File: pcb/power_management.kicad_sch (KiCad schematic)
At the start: 34 parts, among them J3 USB C, J4 BATT, Q2 AO3400A, Q3 AO3401A, SW5 POWER, U4 BQ25619, U5 AP2112K-3.3

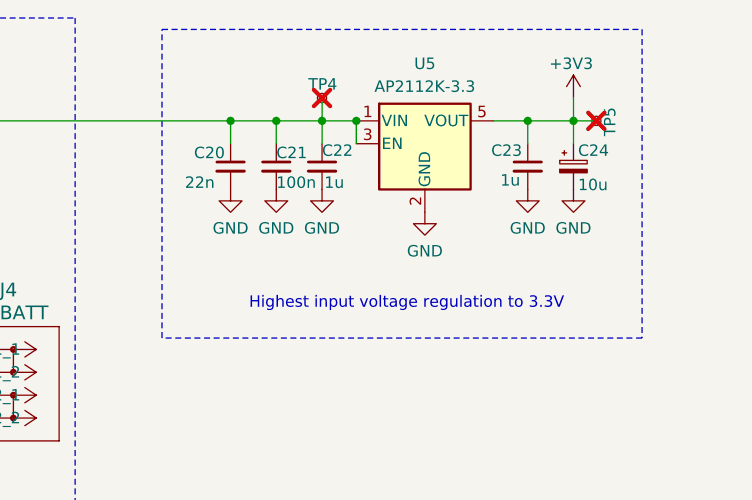
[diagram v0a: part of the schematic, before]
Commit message: a a solder jumper between power output and 3v3
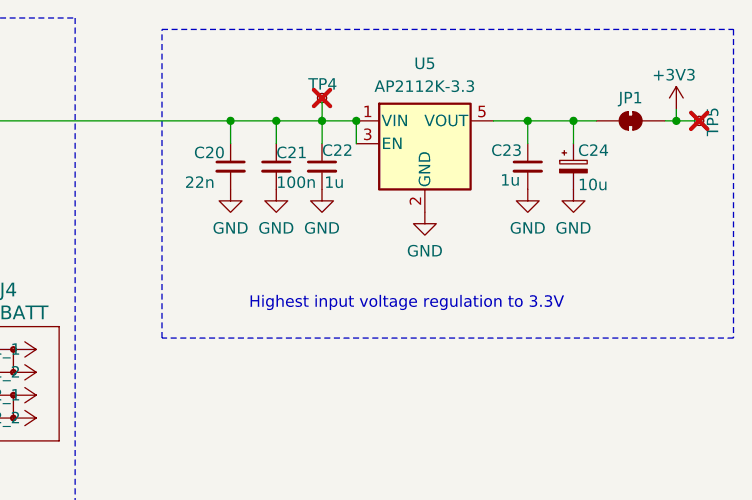
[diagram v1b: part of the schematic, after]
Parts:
- added JP1: SolderJumper_2_Bridged, Jumper:SolderJumper-2_P1.3mm_Bridged_RoundedPad1.0x1.5mm, symbol Jumper:SolderJumper_2_Bridged
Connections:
- net +3V3: now also JP1.2 (B); no longer C23.1, C24.1, U5.5 (VOUT)
- new net: C23.1, C24.1, JP1.1 (A), U5.5 (VOUT)
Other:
- moved on the sheet: TP5
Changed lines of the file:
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@@
 	(rectangle
 		(start 208.28 26.67)
-		(end 261.62 60.96)
+		(end 271.78 60.96)
 		(stroke
 			(width 0)
@@
 	)
 	(junction
+		(at 265.43 36.83)
+		(diameter 0)
+		(color 0 0 0 0)
+	)
+	(junction
 		(at 50.8 76.2)
 		(diameter 0)
@@
 	(wire
 		(pts
-			(xy 254 36.83) (xy 254 34.29)
+			(xy 166.37 53.34) (xy 166.37 54.61)
 		)
 		(stroke
@@
 	(wire
 		(pts
-			(xy 166.37 53.34) (xy 166.37 54.61)
+			(xy 265.43 36.83) (xy 267.97 36.83)
 		)
 		(stroke
@@
 	(wire
 		(pts
+			(xy 264.16 36.83) (xy 265.43 36.83)
+		)
+		(stroke
+			(width 0)
+			(type default)
+		)
+	)
+	(wire
+		(pts
 			(xy 254 36.83) (xy 254 39.37)
 		)
@@
 	(wire
 		(pts
+			(xy 265.43 35.56) (xy 265.43 36.83)
+		)
+		(stroke
+			(width 0)
+			(type default)
+		)
+	)
+	(wire
+		(pts
 			(xy 83.82 125.73) (xy 83.82 137.16)
 		)
@@
 	(symbol
 		(lib_id "power:+3V3")
-		(at 254 34.29 0)
+		(at 265.43 35.56 0)
 		(unit 1)
 		(exclude_from_sim no)
@@
 		(dnp no)
 		(property "Reference" "#PWR043"
-			(at 254 38.1 0)
+			(at 265.43 39.37 0)
 			(effects
 				(font
@@
 		)
 		(property "Value" "+3V3"
-			(at 253.746 30.48 0)
+			(at 265.176 31.75 0)
 			(effects
 				(font
@@
 		)
 		(property "Footprint" ""
-			(at 254 34.29 0)
+			(at 265.43 35.56 0)
 			(effects
 				(font
@@
 		)
 		(property "Datasheet" ""
-			(at 254 34.29 0)
+			(at 265.43 35.56 0)
 			(effects
 				(font
@@
 		)
 		(property "Description" "Power symbol creates a global label with name \"+3V3\""
-			(at 254 34.29 0)
+			(at 265.43 35.56 0)
 			(effects
 				(font
@@
 	)
 	(symbol
+		(lib_id "Jumper:SolderJumper_2_Bridged")
+		(at 260.35 36.83 0)
+		(unit 1)
+		(exclude_from_sim no)
+		(in_bom no)
+		(on_board yes)
+		(dnp no)
+		(property "Reference" "JP1"
+			(at 260.35 34.29 0)
+			(effects
+				(font
+					(size 1.27 1.27)
+				)
+			)
+		)
+		(property "Value" "SolderJumper_2_Bridged"
+			(at 260.35 33.02 0)
+			(effects
+				(font
+					(size 1.27 1.27)
+				)
+				(hide yes)
+			)
+		)
+		(property "Footprint" "Jumper:SolderJumper-2_P1.3mm_Bridged_RoundedPad1.0x1.5mm"
+			(at 260.35 36.83 0)
+			(effects
+				(font
+					(size 1.27 1.27)
+				)
+				(hide yes)
+			)
+		)
+		(property "Datasheet" "~"
+			(at 260.35 36.83 0)
+			(effects
+				(font
+					(size 1.27 1.27)
+				)
+				(hide yes)
+			)
+		)
+		(property "Description" "Solder Jumper, 2-pole, closed/bridged"
+			(at 260.35 36.83 0)
+			(effects
+				(font
+					(size 1.27 1.27)
+				)
+				(hide yes)
+			)
+		)
+		(pin "2"
+		)
+		(pin "1"
+		)
+		(instances
+			(project ""
+				(path "/e47b2519-93ca-4a48-9414-ecc253dd35f5/702fc064-eab2-4b82-8f62-a654ccd28f72"
+					(reference "JP1")
+					(unit 1)
+				)
+			)
+		)
+	)
+	(symbol
 		(lib_id "power:+3V3")
 		(at 128.27 49.53 0)
@@
 	(symbol
 		(lib_id "Connector:TestPoint_Small")
-		(at 256.54 36.83 270)
+		(at 267.97 36.83 270)
 		(unit 1)
 		(exclude_from_sim no)
@@
 		(dnp yes)
 		(property "Reference" "TP5"
-			(at 258.064 35.306 0)
+			(at 269.494 35.306 0)
 			(effects
 				(font
@@
 		)
 		(property "Value" "3.3V"
-			(at 255.2701 38.1 0)
+			(at 266.7001 38.1 0)
 			(effects
 				(font
@@
 		)
 		(property "Footprint" "leany_footprints:TestPoint_Pad_1.0x1.0mm"
-			(at 256.54 41.91 0)
+			(at 267.97 41.91 0)
 			(effects
 				(font
@@
 		)
 		(property "Datasheet" "~"
-			(at 256.54 41.91 0)
+			(at 267.97 41.91 0)
 			(effects
 				(font
@@
 		)
 		(property "Description" "test point"
-			(at 256.54 36.83 0)
+			(at 267.97 36.83 0)
 			(effects
 				(font
@@
 		)
 		(property "Category" ""
-			(at 256.54 36.83 0)
+			(at 267.97 36.83 0)
 			(effects
 				(font
@@
 		)
 		(property "DK_Datasheet_Link" ""
-			(at 256.54 36.83 0)
+			(at 267.97 36.83 0)
 			(effects
 				(font
@@
 		)
 		(property "DK_Detail_Page" ""
-			(at 256.54 36.83 0)
+			(at 267.97 36.83 0)
 			(effects
 				(font
@@
 		)
 		(property "Description_1" ""
-			(at 256.54 36.83 0)
+			(at 267.97 36.83 0)
 			(effects
 				(font
@@
 		)
 		(property "Digi-Key_PN" ""
-			(at 256.54 36.83 0)
+			(at 267.97 36.83 0)
 			(effects
 				(font
@@
 		)
 		(property "Family" ""
-			(at 256.54 36.83 0)
+			(at 267.97 36.83 0)
 			(effects
 				(font
@@
 		)
 		(property "LCSC" ""
-			(at 256.54 36.83 0)
+			(at 267.97 36.83 0)
 			(effects
 				(font
@@
 		)
 		(property "MPN" ""
-			(at 256.54 36.83 0)
+			(at 267.97 36.83 0)
 			(effects
 				(font
@@
 		)
 		(property "Manufacturer" ""
-			(at 256.54 36.83 0)
+			(at 267.97 36.83 0)
 			(effects
 				(font
@@
 		)
 		(property "Status" ""
-			(at 256.54 36.83 0)
+			(at 267.97 36.83 0)
 			(effects
 				(font

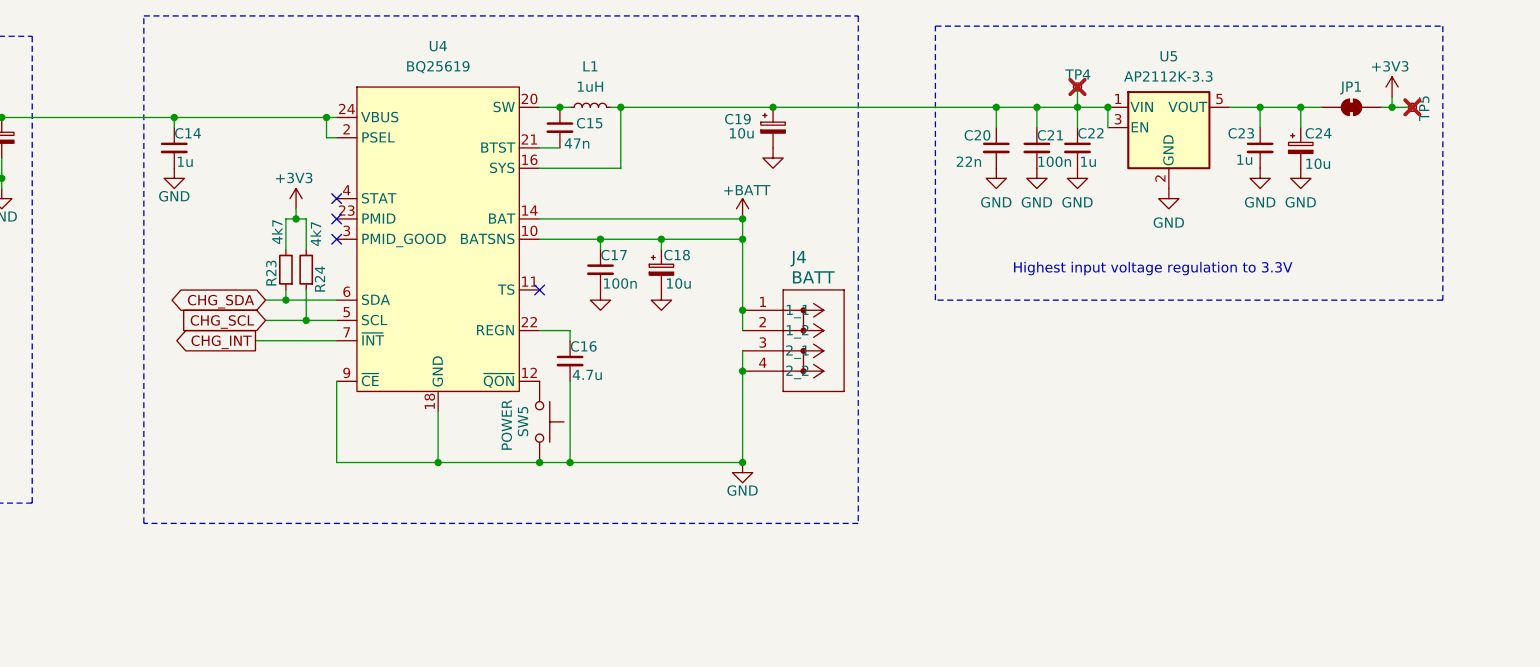
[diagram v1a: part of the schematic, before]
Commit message: add a reverse-voltage protection mosfet
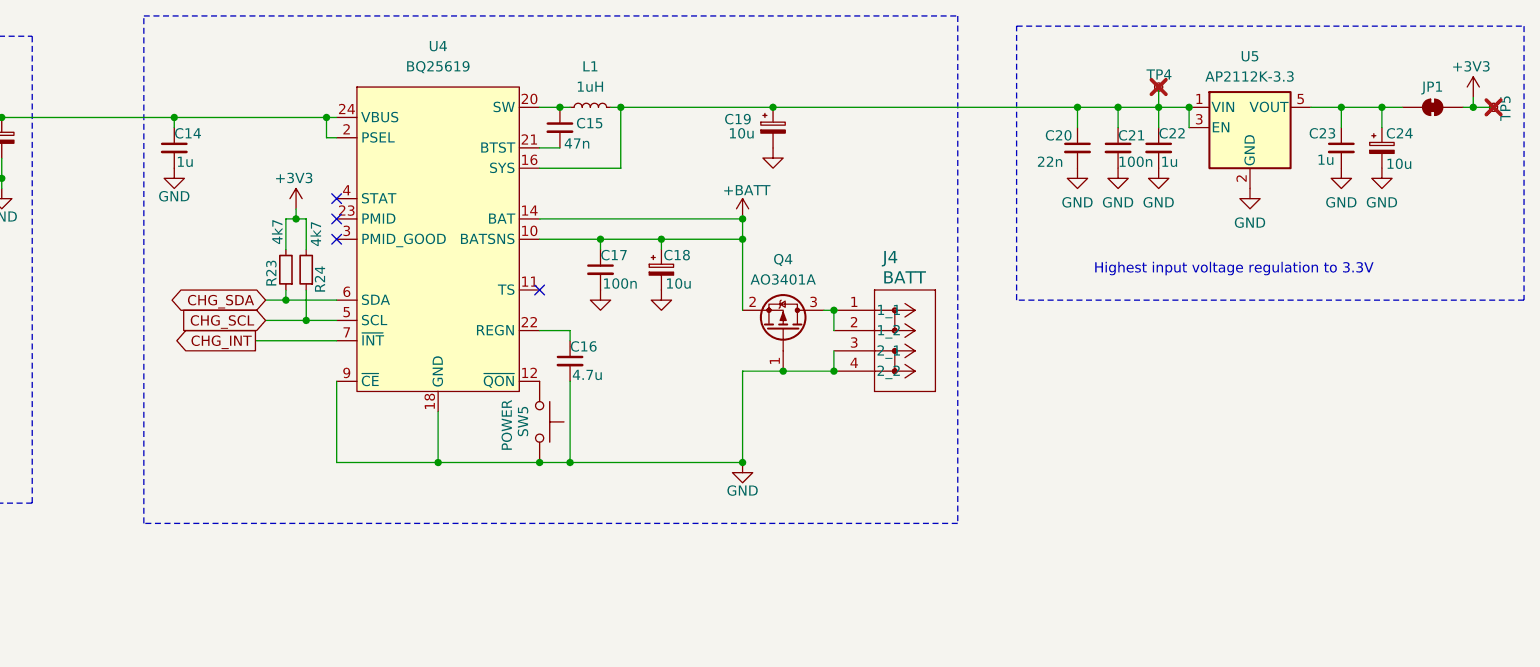
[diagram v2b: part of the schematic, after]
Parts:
- added Q4: AO3401A, Package_TO_SOT_SMD:SOT-23, symbol Transistor_FET:AO3401A
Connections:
- net +BATT: now also Q4.2 (S); no longer J4.1 (1_1), J4.2 (1_2)
- net GND: now also Q4.1 (G)
- new net: J4.1 (1_1), J4.2 (1_2), Q4.3 (D)
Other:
- moved on the sheet: C20, C21, C22, C23, C24, J4, JP1, TP4, TP5, U5

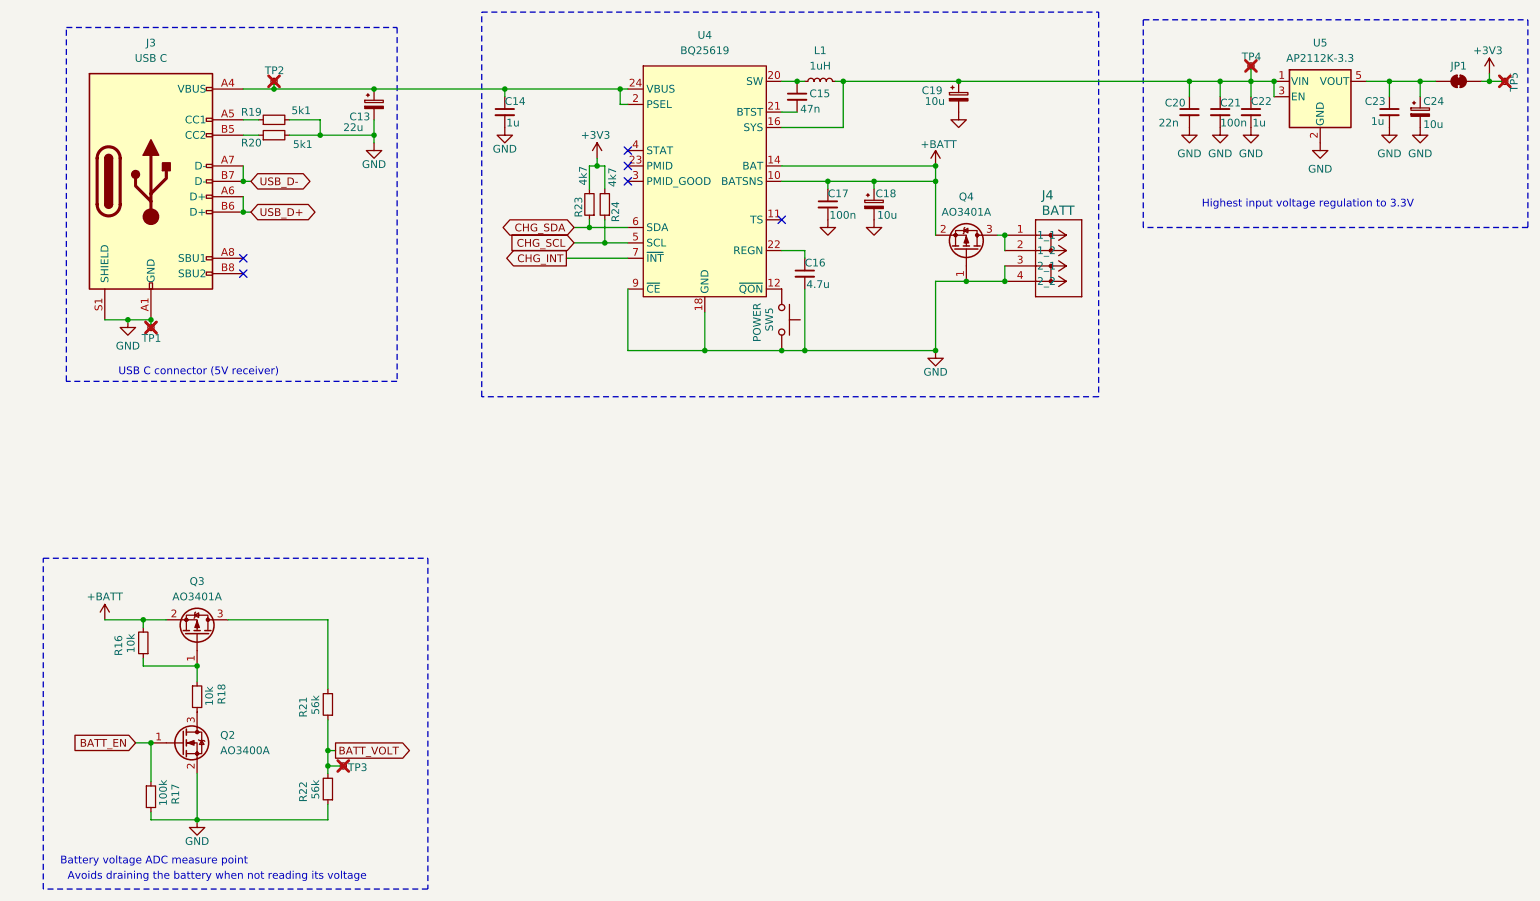
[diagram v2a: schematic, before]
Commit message: replace solder jumper by a test pad near battery
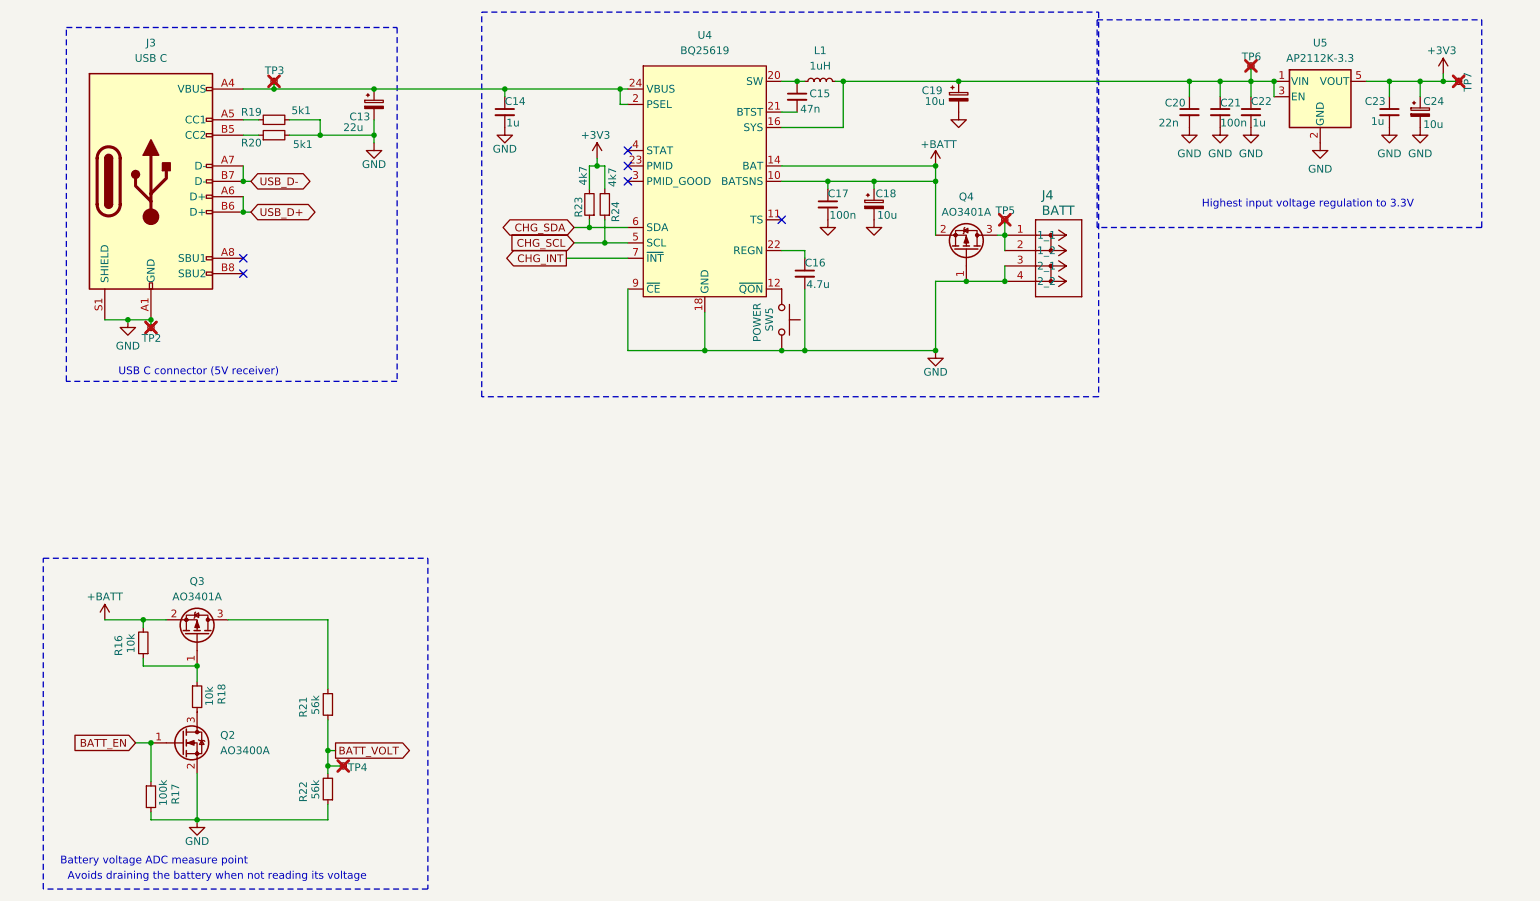
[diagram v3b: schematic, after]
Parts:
- removed JP1: SolderJumper_2_Bridged, Jumper:SolderJumper-2_P1.3mm_Bridged_RoundedPad1.0x1.5mm, symbol Jumper:SolderJumper_2_Bridged
- added TP5: 3.3V, leany_footprints:TestPoint_Pad_1.0x1.0mm, symbol Connector:TestPoint_Small
- renumbered TP1 to TP2, TP2 to TP3, TP3 to TP4, TP4 to TP6, TP5 to TP7
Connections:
- net +3V3: now also C23.1, C24.1, U5.5 (VOUT)
- net at J4.1 (1_1), J4.2 (1_2), Q4.3 (D): now also TP5.1
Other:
- moved on the sheet: TP7

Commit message: start re-designing PCB to 4 layers
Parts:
- C14, C15, C17, C20, C21, C22, C23: footprint Capacitor_SMD:C_0603_1608Metric -> Capacitor_SMD:C_0402_1005Metric
- R16, R17, R18, R19, R20, R21, R22, R23, R24: footprint Resistor_SMD:R_0603_1608Metric -> Resistor_SMD:R_0402_1005Metric
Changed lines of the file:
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@@
 			)
 		)
-		(property "Footprint" "Resistor_SMD:R_0603_1608Metric"
+		(property "Footprint" "Resistor_SMD:R_0402_1005Metric"
 			(at 74.93 43.18 0)
 			(effects
@@
 			)
 		)
-		(property "Footprint" "Capacitor_SMD:C_0603_1608Metric"
+		(property "Footprint" "Capacitor_SMD:C_0402_1005Metric"
 			(at 231.14 41.91 0)
 			(effects
@@
 			)
 		)
-		(property "Footprint" "Resistor_SMD:R_0603_1608Metric"
+		(property "Footprint" "Resistor_SMD:R_0402_1005Metric"
 			(at 83.82 153.67 0)
 			(effects
@@
 			)
 		)
-		(property "Footprint" "Resistor_SMD:R_0603_1608Metric"
+		(property "Footprint" "Resistor_SMD:R_0402_1005Metric"
 			(at 54.61 154.94 0)
 			(effects
@@
 			)
 		)
-		(property "Footprint" "Resistor_SMD:R_0603_1608Metric"
+		(property "Footprint" "Resistor_SMD:R_0402_1005Metric"
 			(at 62.23 138.43 0)
 			(effects
@@
 			)
 		)
-		(property "Footprint" "Capacitor_SMD:C_0603_1608Metric"
+		(property "Footprint" "Capacitor_SMD:C_0402_1005Metric"
 			(at 113.03 41.91 0)
 			(effects
@@
 			)
 		)
-		(property "Footprint" "Resistor_SMD:R_0603_1608Metric"
+		(property "Footprint" "Resistor_SMD:R_0402_1005Metric"
 			(at 83.82 139.7 0)
 			(effects
@@
 			)
 		)
-		(property "Footprint" "Resistor_SMD:R_0603_1608Metric"
+		(property "Footprint" "Resistor_SMD:R_0402_1005Metric"
 			(at 74.93 45.72 0)
 			(effects
@@
 			)
 		)
-		(property "Footprint" "Resistor_SMD:R_0603_1608Metric"
+		(property "Footprint" "Resistor_SMD:R_0402_1005Metric"
 			(at 127 57.15 0)
 			(effects
@@
 			)
 		)
-		(property "Footprint" "Capacitor_SMD:C_0603_1608Metric"
+		(property "Footprint" "Capacitor_SMD:C_0402_1005Metric"
 			(at 166.37 57.15 0)
 			(effects
@@
 			)
 		)
-		(property "Footprint" "Capacitor_SMD:C_0603_1608Metric"
+		(property "Footprint" "Capacitor_SMD:C_0402_1005Metric"
 			(at 236.22 41.91 0)
 			(effects
@@
 			)
 		)
-		(property "Footprint" "Capacitor_SMD:C_0603_1608Metric"
+		(property "Footprint" "Capacitor_SMD:C_0402_1005Metric"
 			(at 226.06 41.91 0)
 			(effects
@@
 			)
 		)
-		(property "Footprint" "Resistor_SMD:R_0603_1608Metric"
+		(property "Footprint" "Resistor_SMD:R_0402_1005Metric"
 			(at 53.34 129.54 0)
 			(effects
@@
 			)
 		)
-		(property "Footprint" "Resistor_SMD:R_0603_1608Metric"
+		(property "Footprint" "Resistor_SMD:R_0402_1005Metric"
 			(at 129.54 57.15 0)
 			(effects
@@
 			)
 		)
-		(property "Footprint" "Capacitor_SMD:C_0603_1608Metric"
+		(property "Footprint" "Capacitor_SMD:C_0402_1005Metric"
 			(at 161.29 39.37 0)
 			(effects
@@
 			)
 		)
-		(property "Footprint" "Capacitor_SMD:C_0603_1608Metric"
+		(property "Footprint" "Capacitor_SMD:C_0402_1005Metric"
 			(at 259.08 41.91 0)
 			(effects

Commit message: update resistors BOM
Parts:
- R16, R18: LCSC C25804 -> C25744
- R17: LCSC C25803 -> C25741
- R19, R20: LCSC C23186 -> C25905
- R21, R22: footprint Resistor_SMD:R_0402_1005Metric -> Resistor_SMD:R_0603_1608Metric
- R23, R24: LCSC C23162 -> C25900
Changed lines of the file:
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@@
 			)
 		)
-		(property "LCSC" "C23186"
+		(property "LCSC" "C25905"
 			(at 74.93 43.18 0)
 			(effects
@@
 			)
 		)
-		(property "Footprint" "Resistor_SMD:R_0402_1005Metric"
+		(property "Footprint" "Resistor_SMD:R_0603_1608Metric"
 			(at 83.82 153.67 0)
 			(effects
@@
 			)
 		)
-		(property "LCSC" "C25803"
+		(property "LCSC" "C25741"
 			(at 54.61 154.94 0)
 			(effects
@@
 			)
 		)
-		(property "LCSC" "C25804"
+		(property "LCSC" "C25744"
 			(at 62.23 138.43 0)
 			(effects
@@
 			)
 		)
-		(property "Footprint" "Resistor_SMD:R_0402_1005Metric"
+		(property "Footprint" "Resistor_SMD:R_0603_1608Metric"
 			(at 83.82 139.7 0)
 			(effects
@@
 			)
 		)
-		(property "LCSC" "C23186"
+		(property "LCSC" "C25905"
 			(at 74.93 45.72 0)
 			(effects
@@
 			)
 		)
-		(property "LCSC" "C23162"
+		(property "LCSC" "C25900"
 			(at 127 57.15 0)
 			(effects
@@
 			)
 		)
-		(property "LCSC" "C25804"
+		(property "LCSC" "C25744"
 			(at 53.34 129.54 0)
 			(effects
@@
 			)
 		)
-		(property "LCSC" "C23162"
+		(property "LCSC" "C25900"
 			(at 129.54 57.15 0)
 			(effects
